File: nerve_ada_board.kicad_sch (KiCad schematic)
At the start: 52 parts, among them J1 TC2050-IDC, J3 USB-C Power Only 6P, J4 Camera, J5 CAN1, J6 CAN2, J7 WS2812B, SW1 SPST, SW2 SPST, SW3 SPDT, SW4 SPST, U1 LD1117S33TR_SOT223, U2 STM32F446RET, U5 XBP9B-DMWT-002, U6 SAM-M10Q, U9 TXB0102DCT, Y1 8M, Y2 32.768K

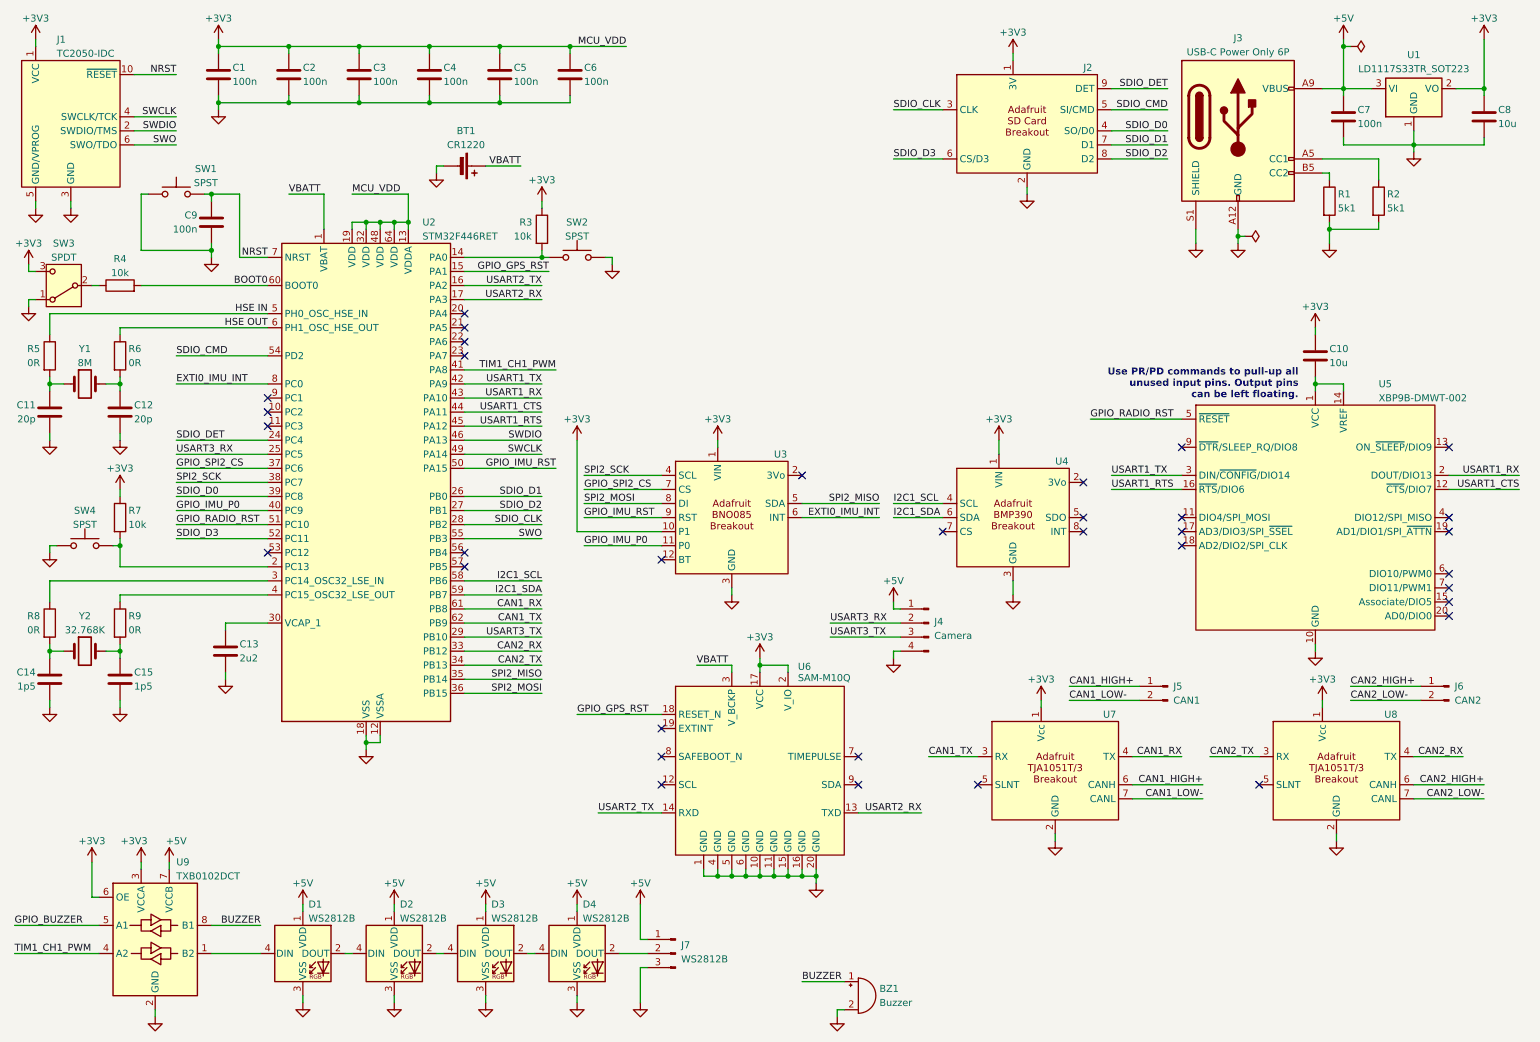
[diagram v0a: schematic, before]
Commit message: Update library, fix power circuits, clean up
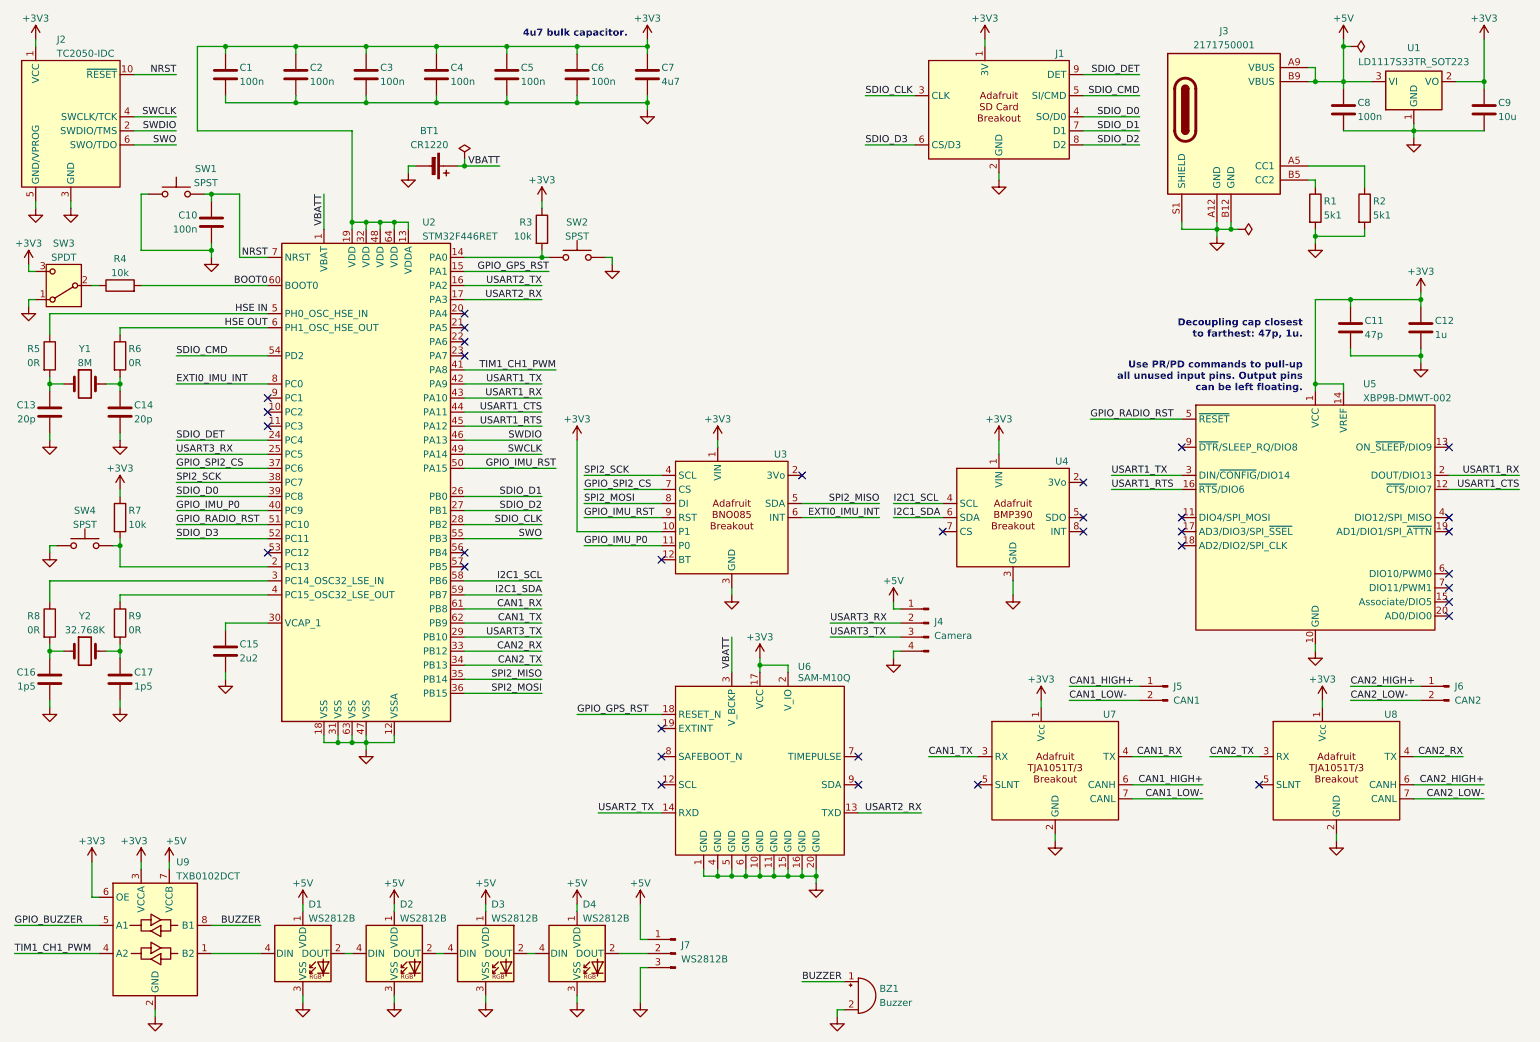
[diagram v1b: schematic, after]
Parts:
- removed C10: 10u, symbol Device:C
- removed J3: USB-C Power Only 6P, symbol Connector:USB_C_Receptacle_PowerOnly_6P
- added C11: 47p, symbol Device:C
- added C12: 1u, symbol Device:C
- added C7: 4u7, symbol Device:C
- added J3: 2171750001, common:molex_2171750001_usb_c_6p, symbol common:molex_2171750001_usb_c_6p
- renumbered C9 to C10, C11 to C13, C12 to C14, C13 to C15, C14 to C16, C15 to C17, C7 to C8, C8 to C9, J2 to J1, J1 to J2
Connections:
- net +3V3: now also U5.1 (VCC), U5.14 (VREF), C11.1, C12.1, C7.1
- net +5V: now also J3.A9 (VBUS), J3.B9 (VBUS)
- net GND: now also C11.2, C12.2, C7.2, J3.A12 (GND), J3.B12 (GND), J3.S1 (SHIELD); no longer U5.8 (Reserved)
- net at R1.1: now also J3.B5 (CC2)
- net at R2.1: now also J3.A5 (CC1)
- now unconnected: J2.7, J2.8, J2.9
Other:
- note added: "4u7 bulk capacitor."
- note added: "Decoupling cap closest to farthest: 47p, 1u."
- moved on the sheet: BT1, C1, C2, C3, C4, C5, C6, C8, C9, J1, R1, R2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

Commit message: Update symbols from library
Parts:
- J1: Distributor (none) -> DigiKey; Distributor Link (none) -> https://www.digikey.ca/en/products/detail/adafruit-industri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; Distributor Part Number (none) -> 1528-4682-ND
- U2: Distributor (none) -> DigiKey; Distributor Link (none) -> https://www.digikey.ca/en/products/detail/stmicroelectronic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; Distributor Part Number (none) -> 497-15376-ND
- U3: Distributor (none) -> DigiKey; Distributor Link (none) -> https://www.digikey.ca/en/products/detail/adafruit-industri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; Distributor Part Number (none) -> 1528-4754-ND
- U4: Distributor (none) -> DigiKey; Distributor Link (none) -> https://www.digikey.ca/en/products/detail/adafruit-industri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; Distributor Part Number (none) -> 1528-4816-ND
- U5: Distributor (none) -> DigiKey; Distributor Link (none) -> https://www.digikey.ca/en/products/detail/digi/XBP9B-DMWT-0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; Distributor Part Number (none) -> 602-1301-ND
- U6: Distributor (none) -> DigiKey; Distributor Link (none) -> https://www.digikey.ca/en/products/detail/u-blox/SAM-M10Q-0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; Distributor Part Number (none) -> 672-SAM-M10Q-00BCT-ND
- U7, U8: Distributor (none) -> DigiKey; Distributor Link (none) -> https://www.digikey.ca/en/products/detail/adafruit-industri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; Distributor Part Number (none) -> 1528-5708-ND
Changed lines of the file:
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@@
 			)
 		)
-		(property "Distributor" ""
+		(property "Distributor" "DigiKey"
 			(at 193.04 104.14 0)
 			(effects
@@
 			)
 		)
-		(property "Distributor Part Number" ""
+		(property "Distributor Part Number" "1528-4816-ND"
 			(at 193.04 104.14 0)
 			(effects
@@
 			)
 		)
-		(property "Distributor Link" ""
+		(property "Distributor Link" "https://www.digikey.ca/en/products/detail/adafruit-industries-llc/4816/13543385?s=N4IgTCBcDaIIYBM4DMBOBXAlgFwAQBYAOARgDYQBdAXyA"
 			(at 193.04 104.14 0)
 			(effects
@@
 			)
 		)
-		(property "Distributor" ""
+		(property "Distributor" "DigiKey"
 			(at 200.66 149.86 0)
 			(effects
@@
 			)
 		)
-		(property "Distributor Part Number" ""
+		(property "Distributor Part Number" "1528-5708-ND"
 			(at 200.66 149.86 0)
 			(effects
@@
 			)
 		)
-		(property "Distributor Link" ""
+		(property "Distributor Link" "https://www.digikey.ca/en/products/detail/adafruit-industries-llc/5708/18716420?s=N4IgTCBcDaIIYBM4DMBOBXAlgFwAQFYB2ABgA4QBdAXyA"
 			(at 200.66 149.86 0)
 			(effects
@@
 			)
 		)
-		(property "Distributor" ""
+		(property "Distributor" "DigiKey"
 			(at 147.32 149.86 0)
 			(effects
@@
 			)
 		)
-		(property "Distributor Part Number" ""
+		(property "Distributor Part Number" "672-SAM-M10Q-00BCT-ND"
 			(at 147.32 149.86 0)
 			(effects
@@
 			)
 		)
-		(property "Distributor Link" ""
+		(property "Distributor Link" "https://www.digikey.ca/en/products/detail/u-blox/SAM-M10Q-00B/16672678?s=N4IgTCBcDaIMoEECyBaJBGADARRAXQF8g"
 			(at 147.32 149.86 0)
 			(effects
@@
 			)
 		)
-		(property "Distributor" ""
+		(property "Distributor" "DigiKey"
 			(at 251.46 149.86 0)
 			(effects
@@
 			)
 		)
-		(property "Distributor Part Number" ""
+		(property "Distributor Part Number" "1528-5708-ND"
 			(at 251.46 149.86 0)
 			(effects
@@
 			)
 		)
-		(property "Distributor Link" ""
+		(property "Distributor Link" "https://www.digikey.ca/en/products/detail/adafruit-industries-llc/5708/18716420?s=N4IgTCBcDaIIYBM4DMBOBXAlgFwAQFYB2ABgA4QBdAXyA"
 			(at 251.46 149.86 0)
 			(effects
@@
 			)
 		)
-		(property "Distributor" ""
+		(property "Distributor" "DigiKey"
 			(at 76.2 97.79 0)
 			(effects
@@
 			)
 		)
-		(property "Distributor Part Number" ""
+		(property "Distributor Part Number" "497-15376-ND"
 			(at 76.2 97.79 0)
 			(effects
@@
 			)
 		)
-		(property "Distributor Link" ""
+		(property "Distributor Link" "https://www.digikey.ca/en/products/detail/stmicroelectronics/STM32F446RET6/5175962"
 			(at 76.2 97.79 0)
 			(effects
@@
 			)
 		)
-		(property "Distributor" ""
+		(property "Distributor" "DigiKey"
 			(at 190.5 30.48 0)
 			(effects
@@
 			)
 		)
-		(property "Distributor Part Number" ""
+		(property "Distributor Part Number" "1528-4682-ND"
 			(at 190.5 30.48 0)
 			(effects
@@
 			)
 		)
-		(property "Distributor Link" ""
+		(property "Distributor Link" "https://www.digikey.ca/en/products/detail/adafruit-industries-llc/4682/12822319?s=N4IgTCBcDaICwDYAcYAEBDAJugZgJwFcBLAFxAF0BfIA"
 			(at 190.5 30.48 0)
 			(effects
@@
 			)
 		)
-		(property "Distributor" ""
+		(property "Distributor" "DigiKey"
 			(at 142.24 104.14 0)
 			(effects
@@
 			)
 		)
-		(property "Distributor Part Number" ""
+		(property "Distributor Part Number" "1528-4754-ND"
 			(at 142.24 104.14 0)
 			(effects
@@
 			)
 		)
-		(property "Distributor Link" ""
+		(property "Distributor Link" "https://www.digikey.ca/en/products/detail/adafruit-industries-llc/4754/13426653?s=N4IgTCBcDaIIYBM4DMBOBXAlgFwAQBYB2AVnxAF0BfIA"
 			(at 142.24 104.14 0)
 			(effects
@@
 			)
 		)
-		(property "Distributor" ""
+		(property "Distributor" "DigiKey"
 			(at 247.65 104.14 0)
 			(effects
@@
 			)
 		)
-		(property "Distributor Part Number" ""
+		(property "Distributor Part Number" "602-1301-ND"
 			(at 247.65 104.14 0)
 			(effects
@@
 			)
 		)
-		(property "Distributor Link" ""
+		(property "Distributor Link" "https://www.digikey.ca/en/products/detail/digi/XBP9B-DMWT-002/3594159?s=N4IgTCBcDaIBoCEAKBOBBaAIgWQOoBV0AGIiAXQF8g"
 			(at 247.65 104.14 0)
 			(effects

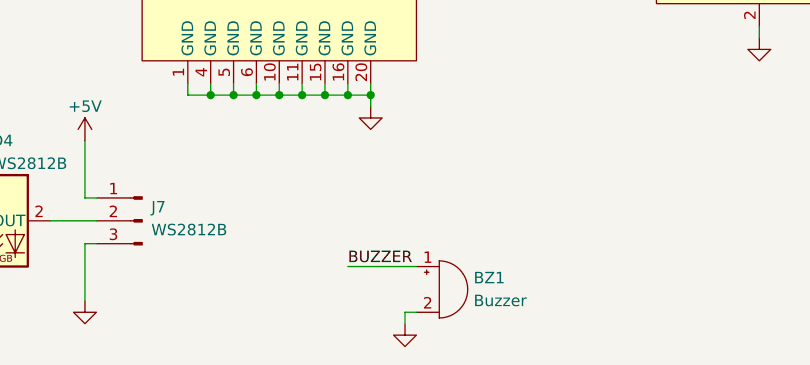
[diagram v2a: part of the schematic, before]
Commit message: Update jumper with library, clean up
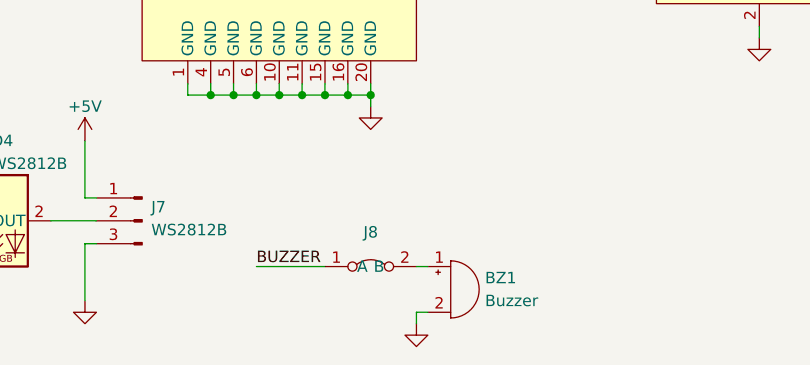
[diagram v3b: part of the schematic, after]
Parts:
- added J8: ~, common:harwin_2p_2-54_jumper_closed, symbol common:harwin_2p_2-54_jumper_closed
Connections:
- net BUZZER: now also J8.1 (A); no longer BZ1.1 (+)
- new net: BZ1.1 (+), J8.2 (B)
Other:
- moved on the sheet: BZ1
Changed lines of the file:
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@@
 	(wire
 		(pts
+			(xy 162.56 187.96) (xy 163.83 187.96)
+		)
+		(stroke
+			(width 0)
+			(type default)
+		)
+	)
+	(wire
+		(pts
 			(xy 147.32 167.64) (xy 147.32 168.91)
 		)
@@
 	(wire
 		(pts
-			(xy 154.94 187.96) (xy 162.56 187.96)
+			(xy 144.78 187.96) (xy 152.4 187.96)
 		)
 		(stroke
@@
 	(wire
 		(pts
-			(xy 161.29 194.31) (xy 161.29 193.04)
+			(xy 162.56 194.31) (xy 162.56 193.04)
 		)
 		(stroke
@@
 	(wire
 		(pts
-			(xy 161.29 193.04) (xy 162.56 193.04)
+			(xy 162.56 193.04) (xy 163.83 193.04)
 		)
 		(stroke
@@
 	)
 	(label "BUZZER"
-		(at 154.94 187.96 0)
+		(at 144.78 187.96 0)
 		(fields_autoplaced yes)
 		(effects
@@
 	(symbol
 		(lib_id "Device:Buzzer")
-		(at 165.1 190.5 0)
+		(at 166.37 190.5 0)
 		(unit 1)
 		(exclude_from_sim no)
@@
 		(fields_autoplaced yes)
 		(property "Reference" "BZ1"
-			(at 168.91 189.2299 0)
+			(at 170.18 189.2299 0)
 			(effects
 				(font
@@
 		)
 		(property "Value" "Buzzer"
-			(at 168.91 191.7699 0)
+			(at 170.18 191.7699 0)
 			(effects
 				(font
@@
 		)
 		(property "Footprint" ""
-			(at 164.465 187.96 90)
+			(at 165.735 187.96 90)
 			(effects
 				(font
@@
 		)
 		(property "Datasheet" "~"
-			(at 164.465 187.96 90)
+			(at 165.735 187.96 90)
 			(effects
 				(font
@@
 		)
 		(property "Description" "Buzzer, polarized"
-			(at 165.1 190.5 0)
+			(at 166.37 190.5 0)
 			(effects
 				(font
@@
 	)
 	(symbol
+		(lib_id "common:harwin_2p_2-54_jumper_closed")
+		(at 157.48 187.96 0)
+		(unit 1)
+		(exclude_from_sim no)
+		(in_bom yes)
+		(on_board yes)
+		(dnp no)
+		(fields_autoplaced yes)
+		(property "Reference" "J8"
+			(at 157.48 184.15 0)
+			(effects
+				(font
+					(size 1.27 1.27)
+				)
+			)
+		)
+		(property "Value" "~"
+			(at 157.48 185.42 0)
+			(effects
+				(font
+					(size 1.27 1.27)
+				)
+			)
+		)
+		(property "Footprint" "common:harwin_2p_2-54_jumper_closed"
+			(at 161.29 190.5 0)
+			(effects
+				(font
+					(size 1.27 1.27)
+				)
+				(hide yes)
+			)
+		)
+		(property "Datasheet" "https://cdn.harwin.com/pdfs/M20-999.pdf"
+			(at 193.04 195.453 0)
+			(effects
+				(font
+					(size 1.27 1.27)
+				)
+				(hide yes)
+			)
+		)
+		(property "Description" "Connector Header Through Hole 2 position 0.100\" (2.54mm)"
+			(at 193.04 191.643 0)
+			(effects
+				(font
+					(size 1.27 1.27)
+				)
+				(hide yes)
+			)
+		)
+		(property "Manufacturer" "Harwin"
+			(at 193.04 186.563 0)
+			(effects
+				(font
+					(size 1.27 1.27)
+				)
+				(hide yes)
+			)
+		)
+		(property "Manufacturer Part Number" "M20-9990246"
+			(at 193.04 186.563 0)
+			(effects
+				(font
+					(size 1.27 1.27)
+				)
+				(hide yes)
+			)
+		)
+		(property "Distributor" "DigiKey"
+			(at 193.04 186.563 0)
+			(effects
+				(font
+					(size 1.27 1.27)
+				)
+				(hide yes)
+			)
+		)
+		(property "Distributor Part Number" "952-2262-ND"
+			(at 193.04 195.453 0)
+			(effects
+				(font
+					(size 1.27 1.27)
+				)
+				(hide yes)
+			)
+		)
+		(property "Distributor Link" "https://www.digikey.ca/en/products/detail/harwin-inc/M20-9990246/3728226"
+			(at 193.04 191.643 0)
+			(effects
+				(font
+					(size 1.27 1.27)
+				)
+				(hide yes)
+			)
+		)
+		(pin "1"
+		)
+		(pin "2"
+		)
+		(instances
+			(project ""
+				(path "/c0277862-b3f2-4e0e-986f-34702f0543f0"
+					(reference "J8")
+					(unit 1)
+				)
+			)
+		)
+	)
+	(symbol
 		(lib_id "power:GND")
 		(at 171.45 129.54 0)
@@
 	(symbol
 		(lib_id "power:GND")
-		(at 161.29 194.31 0)
+		(at 162.56 194.31 0)
 		(unit 1)
 		(exclude_from_sim no)
@@
 		(fields_autoplaced yes)
 		(property "Reference" "#PWR057"
-			(at 161.29 200.66 0)
+			(at 162.56 200.66 0)
 			(effects
 				(font
@@
 		)
 		(property "Value" "GND"
-			(at 161.29 199.39 0)
+			(at 162.56 199.39 0)
 			(effects
 				(font
@@
 		)
 		(property "Footprint" ""
-			(at 161.29 194.31 0)
+			(at 162.56 194.31 0)
 			(effects
 				(font
@@
 		)
 		(property "Datasheet" ""
-			(at 161.29 194.31 0)
+			(at 162.56 194.31 0)
 			(effects
 				(font
@@
 		)
 		(property "Description" "Power symbol creates a global label with name \"GND\" , ground"
-			(at 161.29 194.31 0)
+			(at 162.56 194.31 0)
 			(effects
 				(font
